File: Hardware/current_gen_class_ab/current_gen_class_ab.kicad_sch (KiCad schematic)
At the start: 35 parts, among them J1 Conn_Coaxial, J2 Conn_Coaxial, Q1 NMOS, Q2 NMOS, U1 Opamp_Quad

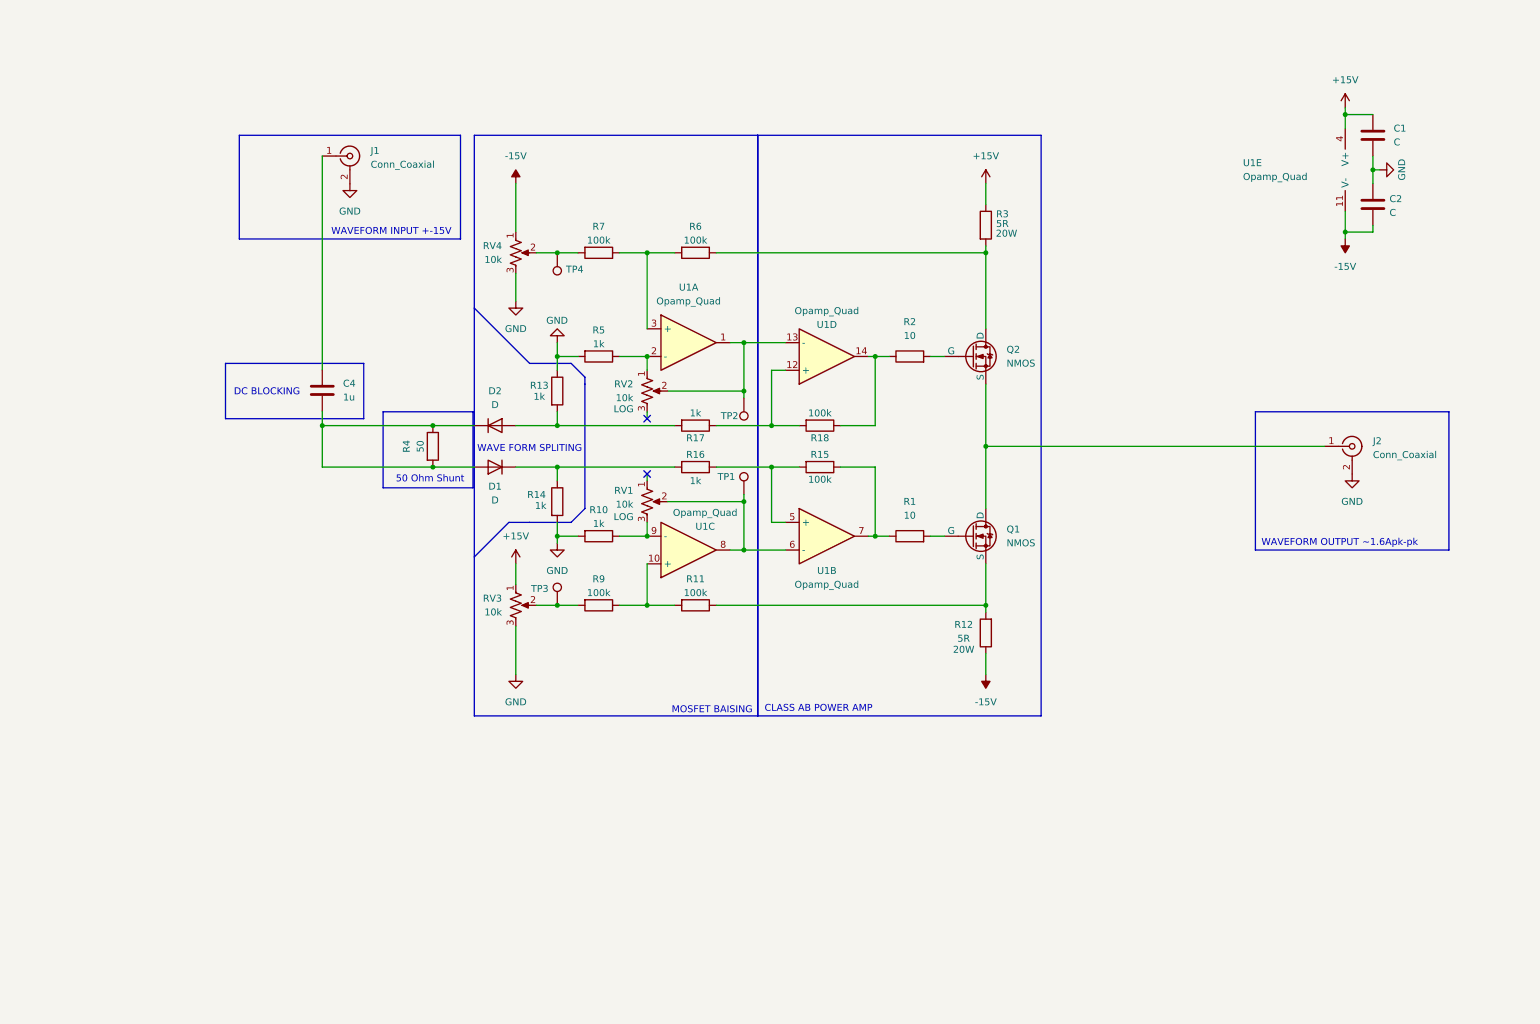
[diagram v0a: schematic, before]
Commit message: started to add parts
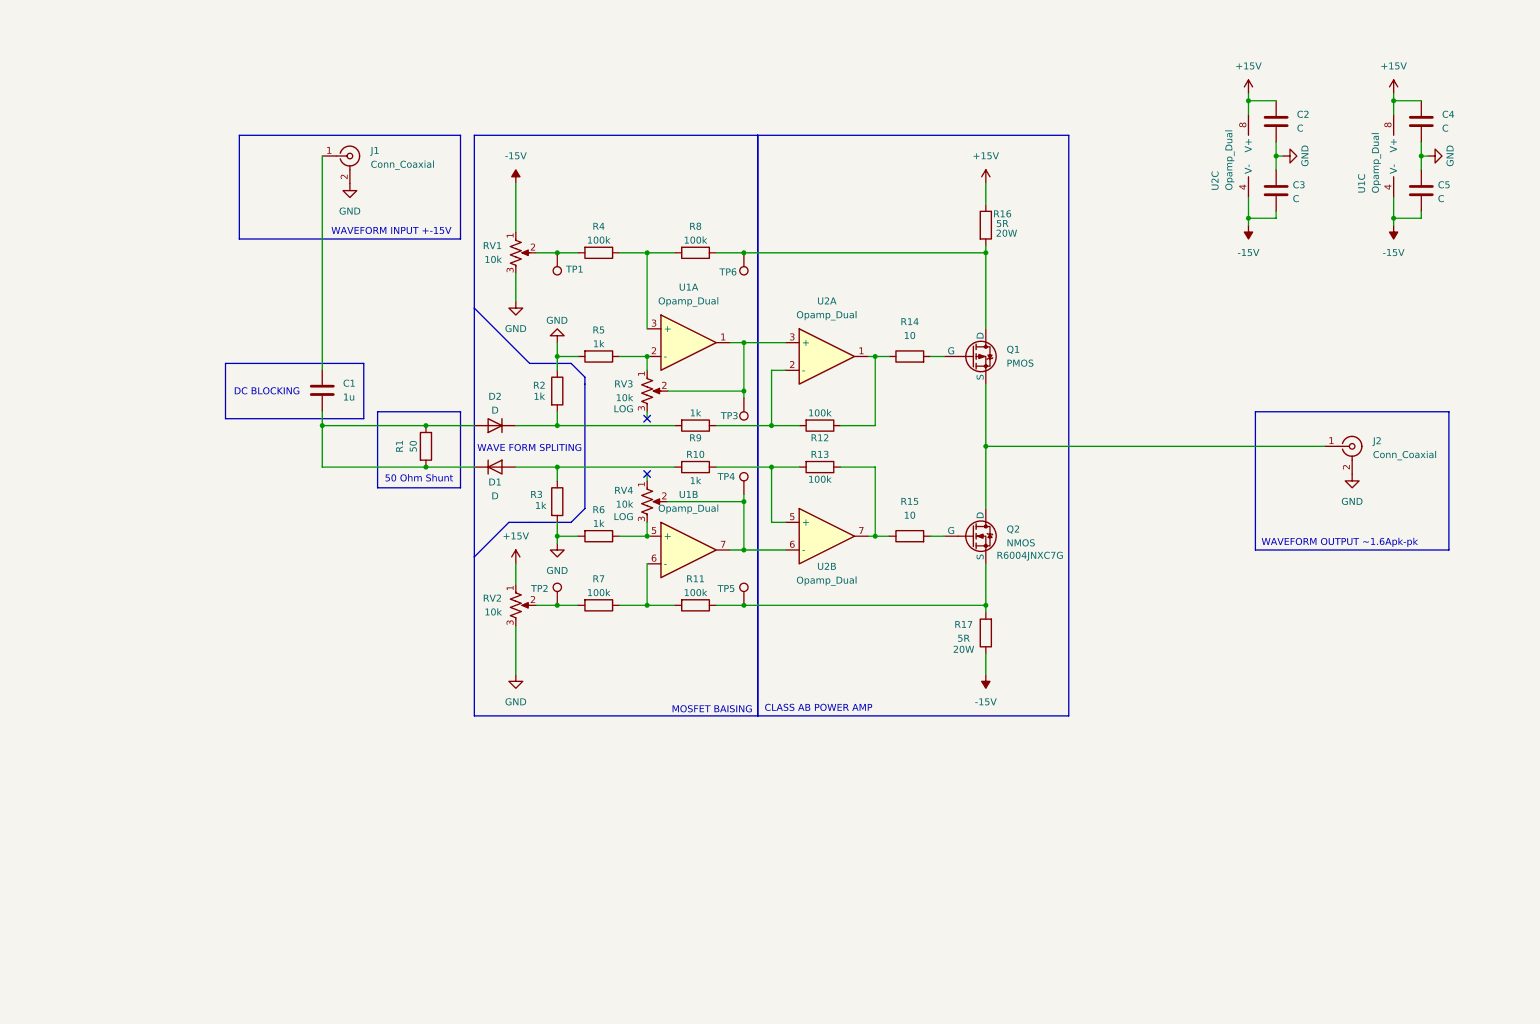
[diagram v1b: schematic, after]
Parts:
- removed Q2: NMOS, symbol Simulation_SPICE:NMOS
- removed U1: Opamp_Quad, symbol Device:Opamp_Quad
- added C2, C3: C, symbol Device:C
- added Q1: PMOS, symbol Simulation_SPICE:PMOS
- added TP5, TP6: TestPoint, symbol Connector:TestPoint
- added U1, U2: Opamp_Dual, symbol Device:Opamp_Dual
- Q2: renamed from Q1; Manufactor Number (none) -> R6004JNXC7G; Supplier Link (none) -> https://www.digikey.co.nz/en/products/detail/rohm-semicondu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
- renumbered C4 to C1, C1 to C4, C2 to C5, D2 to D1, D1 to D2, R4 to R1, R16 to R10, R18 to R12, R15 to R13, R2 to R14, R1 to R15, R3 to R16, R12 to R17, R13 to R2, R14 to R3, R7 to R4, R10 to R6, R9 to R7, R6 to R8, R17 to R9, RV4 to RV1, RV3 to RV2, RV2 to RV3, RV1 to RV4, TP4 to TP1, TP3 to TP2, TP2 to TP3, TP1 to TP4
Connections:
- net +15V: now also C2.2, U1.8 (V+), U2.8 (V+)
- net -15V: now also C3.2, U1.4 (V-), U2.4 (V-)
- net GND: now also C2.1, C3.1
- net at RV4.2, TP4.1: now also U1.7, U2.6 (-)
- net at R6.1, RV4.3: now also U1.5 (+)
- net at R4.1, R8.2: now also U1.3 (+)
- net at R10.2, R3.1: now also D1.2 (A); no longer D2.1 (K)
- net at J2.1 (In), Q2.1 (D): now also Q1.3 (S)
- net at R16.2, R8.1: now also Q1.1 (D), TP6.1
- net at R12.1, R14.1: now also U2.1
- net at R14.2: now also Q1.2 (G)
- net at R10.1, R13.2: now also U2.5 (+)
- net at R13.1, R15.1: now also U2.7
- net at R5.1, RV3.1: now also U1.2 (-)
- net at RV3.2, TP3.1: now also U1.1, U2.3 (+)
- net at R2.2, R9.2: now also D2.1 (K); no longer D1.2 (A)
- net at Q2.3 (S), R11.1, R17.2: now also TP5.1
- net at R11.2, R7.1: now also U1.6 (-)
- net at R12.2, R9.1: now also U2.2 (-)
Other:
- title: (none) -> CURRENT FUNCTION GEN
- moved on the sheet: C4, C5, D1, D2, R1

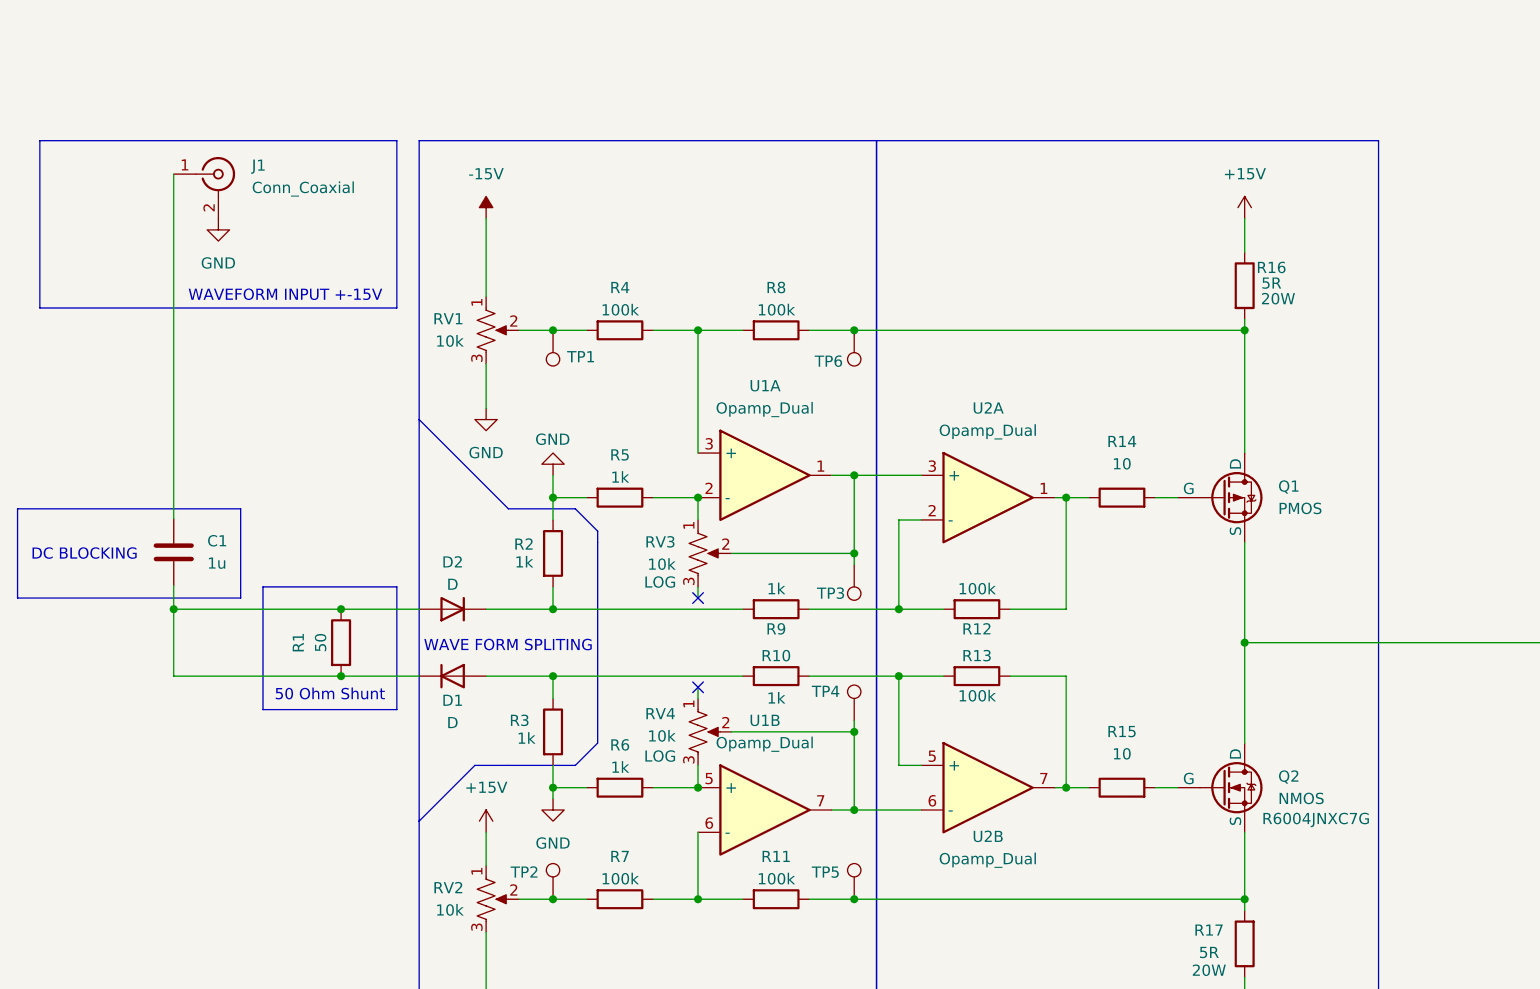
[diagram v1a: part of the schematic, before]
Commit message: added parts for resitors and opamps
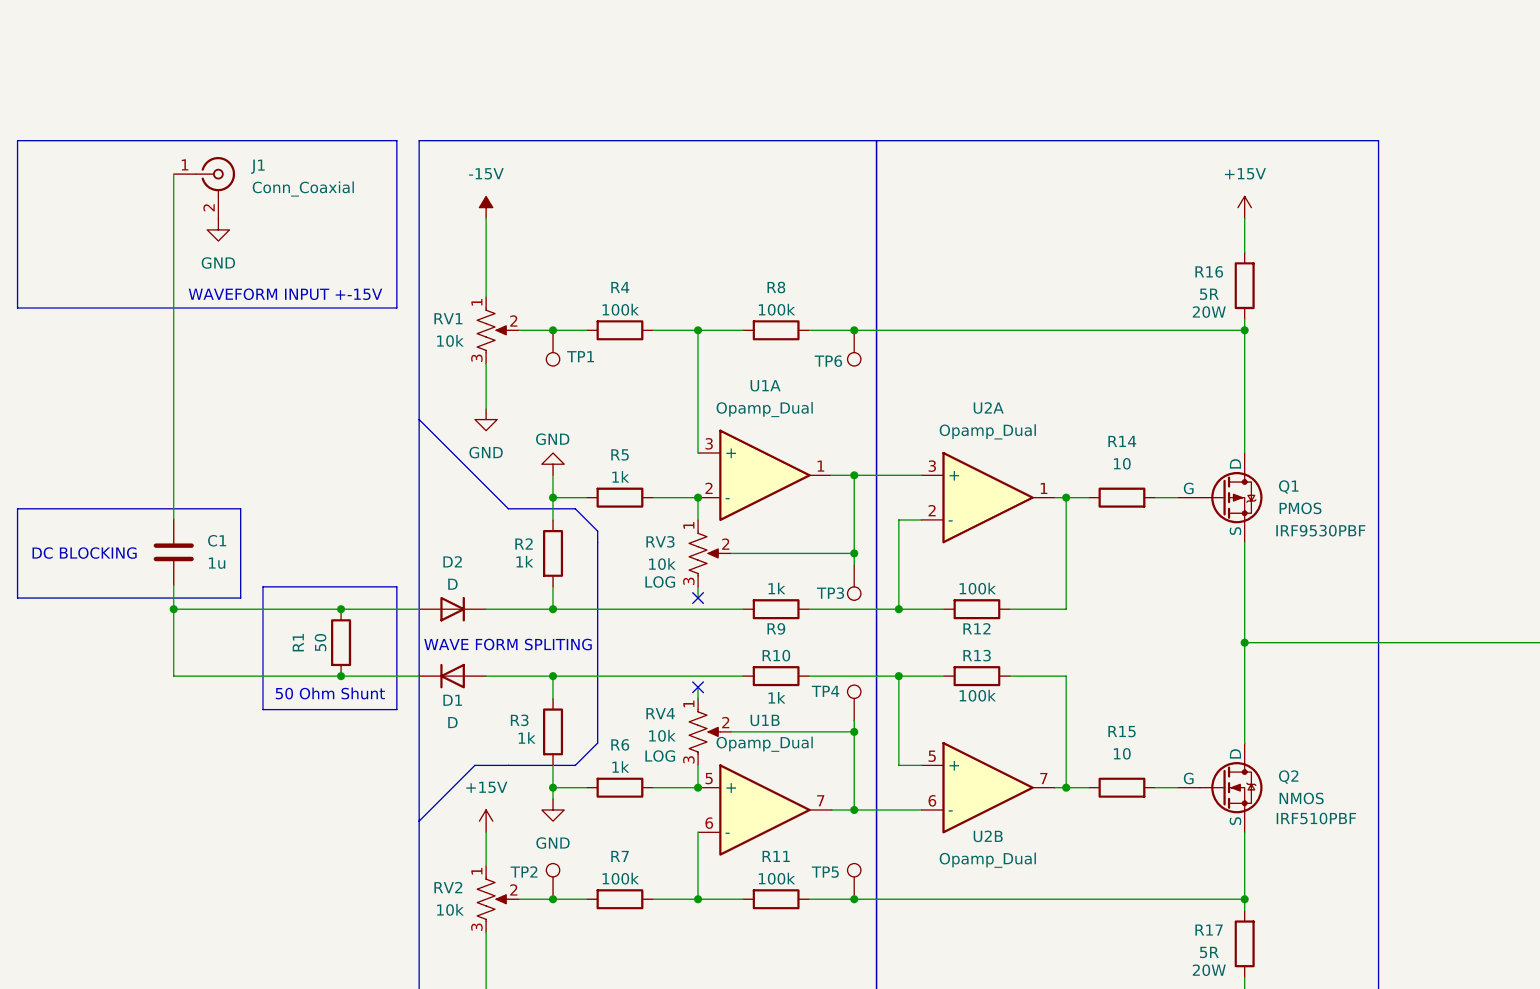
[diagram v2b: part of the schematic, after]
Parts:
- Q1: Manufactor Number (none) -> IRF9530PBF; Supplier Link (none) -> https://www.digikey.co.nz/en/products/detail/vishay-silicon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
- Q2: Manufactor Number R6004JNXC7G -> IRF510PBF; Supplier Link https://www.digikey.co.nz/en/products/detail/rohm-semicondu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 -> https://www.digikey.co.nz/en/products/detail/vishay-silicon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
- R16, R17: Manufactor Number (none) -> PWR220T-35-5R00F; Supplier Link (none) -> https://www.digikey.co.nz/en/products/detail/bourns-inc/PWR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
- U1, U2: Manufactor Number (none) -> LM7372MRX; Supplier Link (none) -> https://www.digikey.co.nz/en/products/detail/texas-instrume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
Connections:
- net +15V: now also R16.2; no longer R16.1
- net at Q1.1 (D), R8.1, TP6.1: now also R16.1; no longer R16.2

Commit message: added rvp
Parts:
- removed D1, D2: D, symbol Device:D
- removed RV1, RV3: 10k, symbol Device:R_Potentiometer_US
- added D1, D2: D_Zener, symbol Device:D_Zener
- added D3: BAV99, Package_TO_SOT_SMD:SOT-23, symbol Diode:BAV99
- added D4, D5: LED, symbol Device:LED
- added F1, F2: Fuse, Fuse:Fuseholder_Clip-5x20mm_Bel_FC-203-22_Lateral_P17.80x5.00mm_D1.17mm_Horizontal, symbol Device:Fuse
- added J3, J4, J5: Conn_01x01_Socket, Connector:Banana_Jack_1Pin, symbol Connector:Conn_01x01_Socket
- added JP1, JP2: Jumper_2_Open, symbol Jumper:Jumper_2_Open
- added Q3: NMOS, Package_TO_SOT_THT:TO-220-3_Horizontal_TabDown, symbol Simulation_SPICE:NMOS
- added Q4: PMOS, Package_TO_SOT_THT:TO-220-3_Horizontal_TabDown, symbol Simulation_SPICE:PMOS
- added R18, R19: 10k, Potentiometer_THT:Potentiometer_Bourns_3296W_Vertical, symbol Device:R_Trim
- added R20, R21: 92k, symbol Device:R
- added R22, R23: 1k, symbol Device:R
- added RV1: 10k, footprints:POT_P120PK-x25_TTE, symbol Device:R_Potentiometer
- added RV3: 10k, Potentiometer_THT:Potentiometer_Bourns_PTV09A-1_Single_Vertical, symbol Device:R_Potentiometer
- added TP7, TP8: TestPoint, symbol Connector:TestPoint
- C1: Notes (none) -> 35v
- C2, C3, C4, C5: value C -> 1u; Notes (none) -> 35v
- J1, J2: footprint (none) -> Connector_Coaxial:BNC_TEConnectivity_1478035_Horizontal
- Q1, Q2: footprint (none) -> Package_TO_SOT_THT:TO-220-3_Horizontal_TabDown
- R12, R13: value 100k -> 92k
- RV2: footprint (none) -> footprints:POT_P120PK-x25_TTE; symbol Device:R_Potentiometer_US -> Device:R_Potentiometer; Manufactor Number (none) -> P120PK-Y25BR10K; Supplier Link (none) -> https://www.digikey.co.nz/en/products/detail/tt-electronics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
- RV4: footprint (none) -> Potentiometer_THT:Potentiometer_Bourns_PTV09A-1_Single_Vertical; symbol Device:R_Potentiometer_US -> Device:R_Potentiometer; Manufactor Number (none) -> PTV09A-4025S-A103; Supplier Link (none) -> https://www.digikey.co.nz/en/products/detail/bourns-inc/PTV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
- TP1, TP3, TP6: now left out of the parts list
- TP2: Notes (none) -> + V_OFFSET; now left out of the parts list
- TP4: Notes (none) -> - DIFF BASE; now left out of the parts list
- TP5: Notes (none) -> - VOLTAGE FEEDBACK; now left out of the parts list
- U1, U2: footprint (none) -> Package_SO:SOIC-8-1EP_3.9x4.9mm_P1.27mm_EP2.29x3mm_ThermalVias
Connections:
- net +15V: now also C5.2, D1.1 (K), D4.2 (A), JP1.1 (A), Q4.1 (D); no longer C4.2
- net -15V: now also C3.1, C4.1, D2.2 (A), D5.1 (K), JP2.2 (B), Q3.3 (S), RV1.1; no longer C3.2, C5.2
- net GND: now also C3.2, C4.2, R1.2, J4.1 (Pin_1), R20.2, R21.1, R22.2, R23.2, RV1.3; no longer C3.1, C4.1
- net at R4.2, TP1.1: now also RV1.2
- net at R2.2, R9.2: now also D3.2 (A)
- net at R14.1, U2.1: now also R19.2, TP7.1; no longer R12.1
- net at TP3.1, U1.1, U2.3 (+): now also RV3.2
- net at C1.1: now also R1.1, D3.3 (K); no longer J1.1 (In)
- net at R10.2, R3.1: now also D3.1 (K)
- net at R5.1, U1.2 (-): now also RV3.1
- net at R15.1, U2.7: now also R18.2, TP8.1; no longer R13.1
- new net: D4.1 (K), R22.1
- new net: D1.2 (A), Q4.2 (G), R21.2
- new net: F1.1, JP1.2 (B), Q4.3 (S)
- new net: F1.2, J3.1 (Pin_1)
- new net: D5.2 (A), R23.1
- new net: F2.2, J5.1 (Pin_1)
- new net: F2.1, JP2.1 (A), Q3.1 (D)
- new net: R13.1, R18.1
- new net: D2.1 (K), Q3.2 (G), R20.1
- new net: R12.1, R19.1
- now unconnected: C1.2
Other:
- note added: "100x gain trimmer"
- note added: "POWER"
- note added: "USE: 1. MESURE "VOLTAGE FEEDBACK" and take its max for the negitive rail min for the positive rail and set "V_OFFSET" on the given side to that value 2. MESURE "DIIF BASE" and make sure its max value is -15V for the negitive side +15V for the positive side turing RV3/4 as needed 3. MESURE the output voltage across a dummy load set the 100x gain trimmer to shrink the crossing"
- moved on the sheet: C2, R1, R12, R13, U1C, U2C
